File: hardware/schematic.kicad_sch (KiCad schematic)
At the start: 11 parts, among them J1 Connector_3, J2 Connector_2, J3 Connector_1, J4 Connector_4, J5 Connector_5, J6 Connector_6, U2 Nordic nRF52840 USB Dongle

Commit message: Small schematic update
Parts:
- removed J5: Connector_5, symbol Connector_Generic:Conn_01x03
- added J?: Connector_1, symbol Connector_Generic:Conn_01x04
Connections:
- net +5V: now also J?.1 (Pin_1)
- net Display-UART2_RX: now also J?.3 (Pin_3)
- net Display-UART2_TX: now also J?.2 (Pin_2)
- net GND: now also J?.4 (Pin_4)
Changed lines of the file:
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@@
+    (stroke (width 0) (type default) (color 0 0 0 0))
+  )
+  (wire (pts (xy 300.482 161.544) (xy 306.07 161.544))
     (stroke (width 0) (type default) (color 0 0 0 0))
   )
@@
   (label "SCLK" (at 184.8104 114.046 0)
     (effects (font (size 1.27 1.27)) (justify left bottom))
+  )
+  (label "+5V" (at 306.07 161.544 180)
+    (effects (font (size 1.27 1.27)) (justify right bottom))
   )
   (label "MISO" (at 285.3436 118.11 0)
@@
     (pin "1")
   )
-  (symbol (lib_id "Connector_Generic:Conn_01x03") (at 295.402 166.624 0) (mirror y) (unit 1)
-    (in_bom yes) (on_board yes)
-    (property "Reference" "J5" (id 0) (at 295.402 157.226 0)
-      (effects (font (size 1.27 1.27)) hide)
-    )
-    (property "Value" "Connector_5" (id 1) (at 292.1 167.132 90))
-    (property "Footprint" "" (id 2) (at 295.402 166.624 0)
-      (effects (font (size 1.27 1.27)) hide)
-    )
-    (property "Datasheet" "~" (id 3) (at 295.402 166.624 0)
+  (symbol (lib_id "Connector_Generic:Conn_01x04") (at 295.402 164.084 0) (mirror y) (unit 1)
+    (in_bom yes) (on_board yes)
+    (property "Reference" "J?" (id 0) (at 295.402 176.2252 0)
+      (effects (font (size 1.27 1.27)) hide)
+    )
+    (property "Value" "Connector_1" (id 1) (at 292.1 165.608 90))
+    (property "Footprint" "" (id 2) (at 295.402 164.084 0)
+      (effects (font (size 1.27 1.27)) hide)
+    )
+    (property "Datasheet" "~" (id 3) (at 295.402 164.084 0)
       (effects (font (size 1.27 1.27)) hide)
     )
@@
     (pin "2")
     (pin "3")
+    (pin "4")
   )
   (symbol (lib_id "Connector_Generic:Conn_01x02") (at 205.486 169.418 0) (mirror y) (unit 1)
@@
       (reference "J4") (unit 1) (value "Connector_4") (footprint "")
     )
-    (path "/3b6cb90e-f9fc-423a-bfb7-da052d8cf8af"
-      (reference "J5") (unit 1) (value "Connector_5") (footprint "")
-    )
     (path "/8de58a5f-d840-4c70-b7ae-d0148d4d329e"
       (reference "J6") (unit 1) (value "Connector_6") (footprint "")
     )
+    (path "/3b32823d-13b3-456f-8083-472773d66322"
+      (reference "J?") (unit 1) (value "Connector_1") (footprint "")
+    )
     (path "/00000000-0000-0000-0000-000062499af1"

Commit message: Removed not needed 2 pull up resistors. Corrected power for throttle, should be 3.3V
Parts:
- removed R2, R3: 100K, symbol Device:R
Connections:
- net +3.3V: now also J2.1 (Pin_1)
- net +5V: no longer J2.1 (Pin_1)

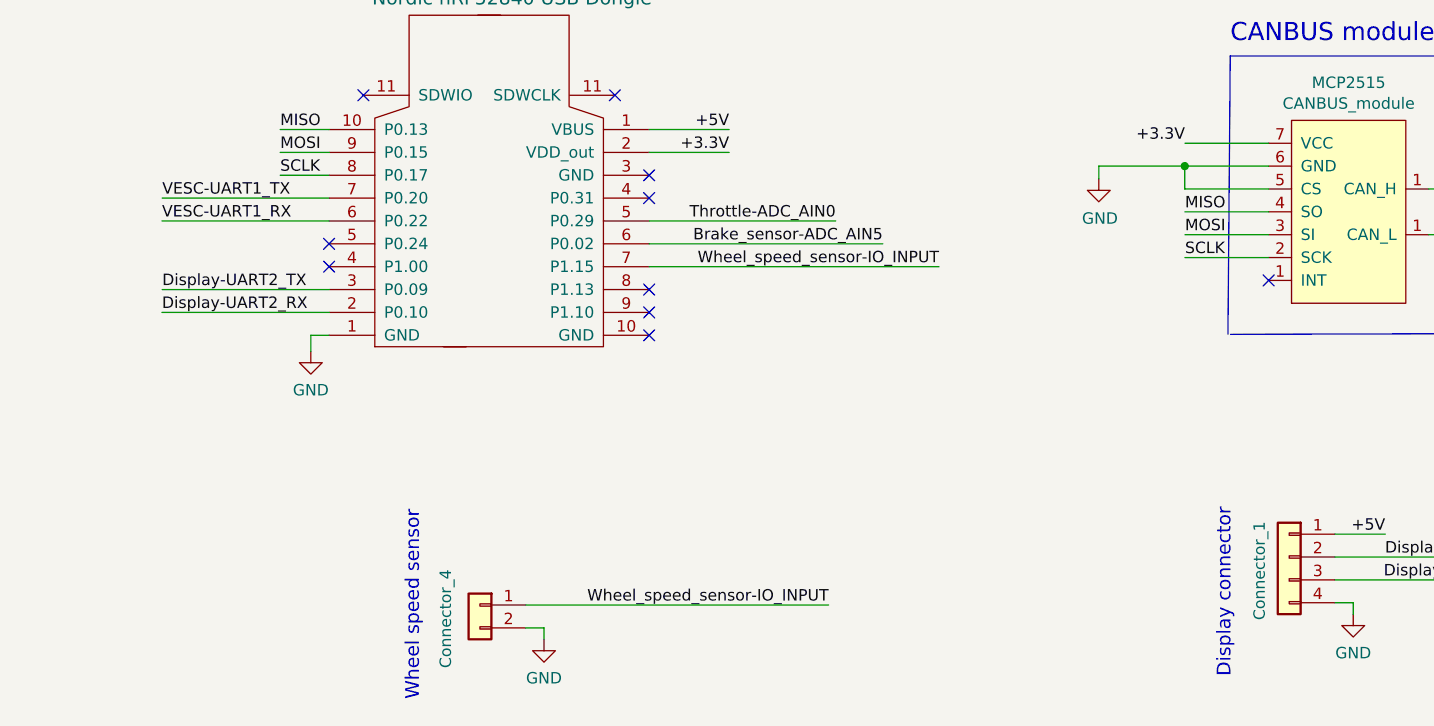
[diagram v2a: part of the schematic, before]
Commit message: Changed SPI pin to a more logical one - changed on firmware and on the schematic
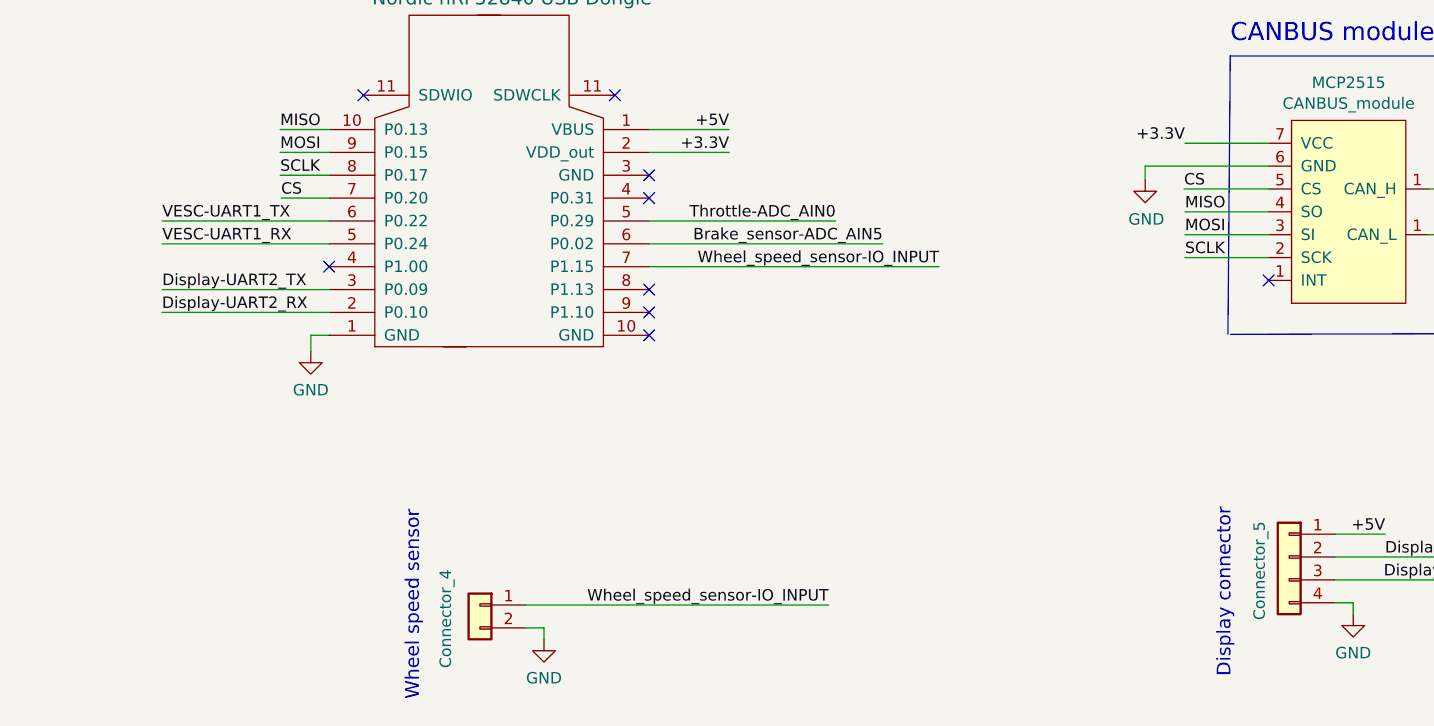
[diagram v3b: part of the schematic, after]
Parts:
- J?: value Connector_1 -> Connector_5
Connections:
- net GND: no longer MCP2515.5 (CS)
- net VESC-UART1_RX: now also U2.5 (P0.29); no longer U2.6 (P0.22)
- net VESC-UART1_TX: now also U2.6 (P0.22); no longer U2.7 (P1.15)
- new net CS: MCP2515.5 (CS), U2.7 (P1.15)
- no-connect marks 10 -> 9
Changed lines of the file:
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@@
 (kicad_sch (version 20211123) (generator eeschema)
   (paper "A3")
-  (junction (at 285.3182 113.03) (diameter 0) (color 0 0 0 0)
-  )
   (junction (at 126.492 129.794) (diameter 0) (color 0 0 0 0)
   )
-  (no_connect (at 190.246 121.666))
   (no_connect (at 221.996 105.156))
   (no_connect (at 294.64 125.73))
@@
     (stroke (width 0) (type default) (color 0 0 0 0))
   )
-  (wire (pts (xy 171.6786 119.126) (xy 190.246 119.126))
-    (stroke (width 0) (type default) (color 0 0 0 0))
-  )
-  (wire (pts (xy 275.7678 113.03) (xy 285.3182 113.03))
+  (wire (pts (xy 280.924 113.03) (xy 294.64 113.03))
     (stroke (width 0) (type default) (color 0 0 0 0))
   )
@@
     (stroke (width 0) (type default) (color 0 0 0 0))
   )
-  (wire (pts (xy 285.3182 113.03) (xy 294.64 113.03))
-    (stroke (width 0) (type default) (color 0 0 0 0))
-  )
   (polyline (pts (xy 290.3728 100.7872) (xy 290.1188 131.699))
     (stroke (width 0) (type default) (color 0 0 0 0))
@@
     (stroke (width 0) (type default) (color 0 0 0 0))
   )
-  (wire (pts (xy 285.3182 115.57) (xy 285.3182 113.03))
-    (stroke (width 0) (type default) (color 0 0 0 0))
-  )
   (wire (pts (xy 302.006 153.924) (xy 307.594 153.924))
     (stroke (width 0) (type default) (color 0 0 0 0))
@@
     (stroke (width 0) (type default) (color 0 0 0 0))
   )
-  (wire (pts (xy 275.7678 113.03) (xy 275.7678 114.4524))
+  (wire (pts (xy 280.924 113.03) (xy 280.924 114.554))
     (stroke (width 0) (type default) (color 0 0 0 0))
   )
@@
     (stroke (width 0) (type default) (color 0 0 0 0))
   )
+  (wire (pts (xy 190.246 116.586) (xy 184.912 116.586))
+    (stroke (width 0) (type default) (color 0 0 0 0))
+  )
   (wire (pts (xy 225.806 108.966) (xy 234.696 108.966))
     (stroke (width 0) (type default) (color 0 0 0 0))
@@
     (stroke (width 0) (type default) (color 0 0 0 0))
   )
+  (wire (pts (xy 171.704 121.666) (xy 190.246 121.666))
+    (stroke (width 0) (type default) (color 0 0 0 0))
+  )
+  (wire (pts (xy 171.704 119.126) (xy 190.246 119.126))
+    (stroke (width 0) (type default) (color 0 0 0 0))
+  )
   (wire (pts (xy 118.491 165.4048) (xy 120.523 165.4048))
     (stroke (width 0) (type default) (color 0 0 0 0))
@@
     (stroke (width 0) (type default) (color 0 0 0 0))
   )
-  (wire (pts (xy 285.3182 115.57) (xy 294.64 115.57))
-    (stroke (width 0) (type default) (color 0 0 0 0))
-  )
   (wire (pts (xy 312.42 115.57) (xy 326.39 115.57))
     (stroke (width 0) (type default) (color 0 0 0 0))
@@
     (stroke (width 0) (type default) (color 0 0 0 0))
   )
+  (wire (pts (xy 294.64 115.57) (xy 285.242 115.57))
+    (stroke (width 0) (type default) (color 0 0 0 0))
+  )
   (wire (pts (xy 118.237 101.9048) (xy 120.269 101.9048))
     (stroke (width 0) (type default) (color 0 0 0 0))
   )
   (wire (pts (xy 126.492 129.794) (xy 126.492 131.572))
-    (stroke (width 0) (type default) (color 0 0 0 0))
-  )
-  (wire (pts (xy 171.704 116.586) (xy 190.246 116.586))
     (stroke (width 0) (type default) (color 0 0 0 0))
   )
@@
     (effects (font (size 1.27 1.27)) (justify left bottom))
   )
-  (label "VESC-UART1_RX" (at 171.6786 119.126 0)
-    (effects (font (size 1.27 1.27)) (justify left bottom))
-  )
   (label "+5V" (at 123.825 94.2848 180)
     (effects (font (size 1.27 1.27)) (justify right bottom))
@@
     (effects (font (size 1.27 1.27)) (justify left bottom))
   )
+  (label "VESC-UART1_RX" (at 171.704 121.666 0)
+    (effects (font (size 1.27 1.27)) (justify left bottom))
+  )
   (label "CAN_H" (at 317.754 115.57 0)
     (effects (font (size 1.27 1.27)) (justify left bottom))
@@
     (effects (font (size 1.27 1.27)) (justify left bottom))
   )
+  (label "VESC-UART1_TX" (at 171.704 119.126 0)
+    (effects (font (size 1.27 1.27)) (justify left bottom))
+  )
   (label "VESC-UART1_RX" (at 135.763 96.8248 180)
     (effects (font (size 1.27 1.27)) (justify right bottom))
@@
     (effects (font (size 1.27 1.27)) (justify right bottom))
   )
-  (label "VESC-UART1_TX" (at 171.704 116.586 0)
-    (effects (font (size 1.27 1.27)) (justify left bottom))
-  )
   (label "Wheel_speed_sensor-IO_INPUT" (at 258.0132 124.206 180)
     (effects (font (size 1.27 1.27)) (justify right bottom))
   )
+  (label "CS" (at 184.912 116.586 0)
+    (effects (font (size 1.27 1.27)) (justify left bottom))
+  )
   (label "Throttle-ADC_AIN0" (at 246.5324 119.126 180)
     (effects (font (size 1.27 1.27)) (justify right bottom))
@@
   )
   (label "SCLK" (at 285.3436 123.19 0)
+    (effects (font (size 1.27 1.27)) (justify left bottom))
+  )
+  (label "CS" (at 285.242 115.57 0)
     (effects (font (size 1.27 1.27)) (justify left bottom))
   )
@@
     (pin "7")
   )
-  (symbol (lib_id "power:GND") (at 275.7678 114.4524 0) (unit 1)
-    (in_bom yes) (on_board yes)
-    (property "Reference" "#PWR04" (id 0) (at 275.7678 120.8024 0)
-      (effects (font (size 1.27 1.27)) hide)
-    )
-    (property "Value" "GND" (id 1) (at 275.8948 118.8466 0))
-    (property "Footprint" "" (id 2) (at 275.7678 114.4524 0)
-      (effects (font (size 1.27 1.27)) hide)
-    )
-    (property "Datasheet" "" (id 3) (at 275.7678 114.4524 0)
+  (symbol (lib_id "power:GND") (at 280.924 114.554 0) (unit 1)
+    (in_bom yes) (on_board yes)
+    (property "Reference" "#PWR04" (id 0) (at 280.924 120.904 0)
+      (effects (font (size 1.27 1.27)) hide)
+    )
+    (property "Value" "GND" (id 1) (at 281.051 118.9482 0))
+    (property "Footprint" "" (id 2) (at 280.924 114.554 0)
+      (effects (font (size 1.27 1.27)) hide)
+    )
+    (property "Datasheet" "" (id 3) (at 280.924 114.554 0)
       (effects (font (size 1.27 1.27)) hide)
     )
@@
       (effects (font (size 1.27 1.27)) hide)
     )
-    (property "Value" "Connector_1" (id 1) (at 293.624 157.988 90))
+    (property "Value" "Connector_5" (id 1) (at 293.624 157.988 90))
     (property "Footprint" "" (id 2) (at 296.926 156.464 0)
       (effects (font (size 1.27 1.27)) hide)
@@
     )
     (path "/3b32823d-13b3-456f-8083-472773d66322"
-      (reference "J?") (unit 1) (value "Connector_1") (footprint "")
+      (reference "J?") (unit 1) (value "Connector_5") (footprint "")
     )
     (path "/00000000-0000-0000-0000-000062499af1"

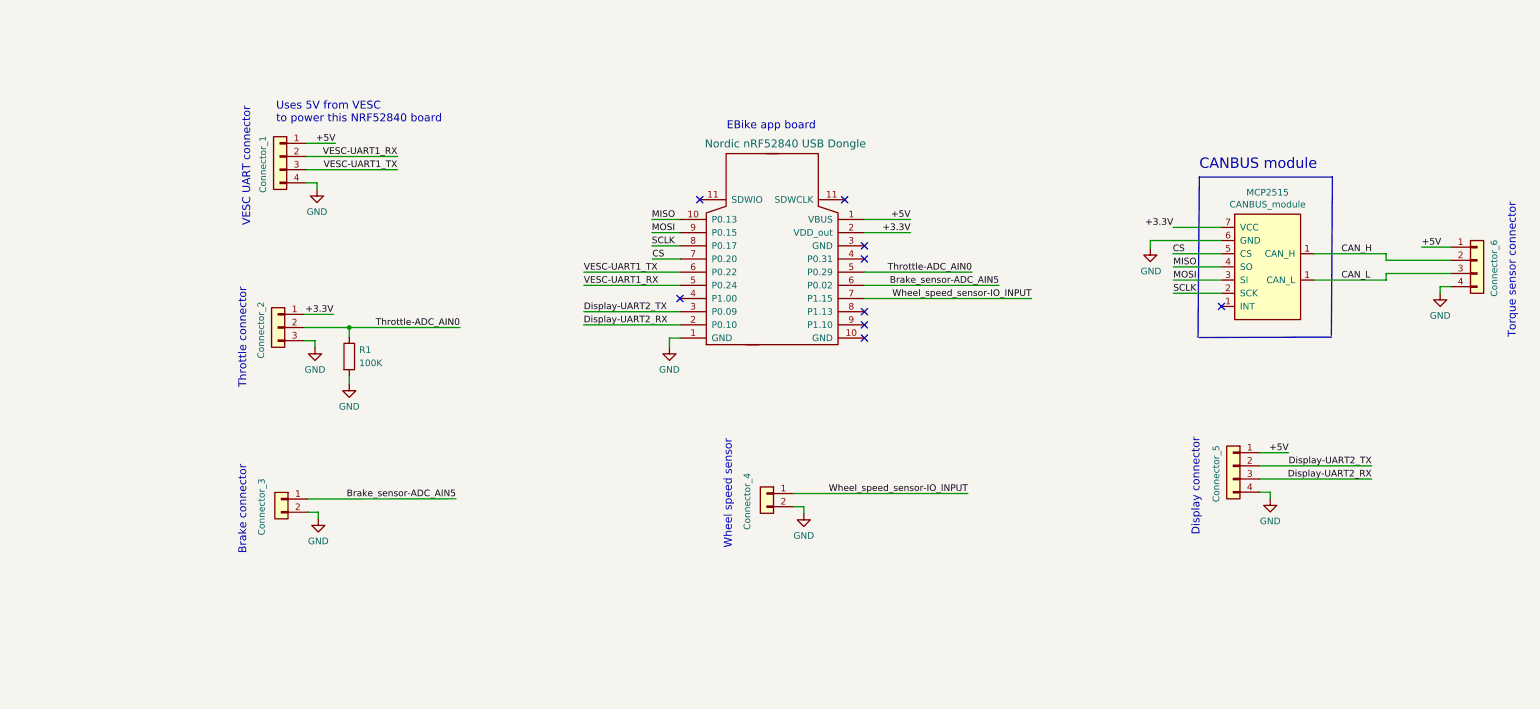
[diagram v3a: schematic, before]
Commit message: Updated schematic, added ESP32-S3 board and removed NRF52840. Added circuit to the motor temperature sensor (not tested).
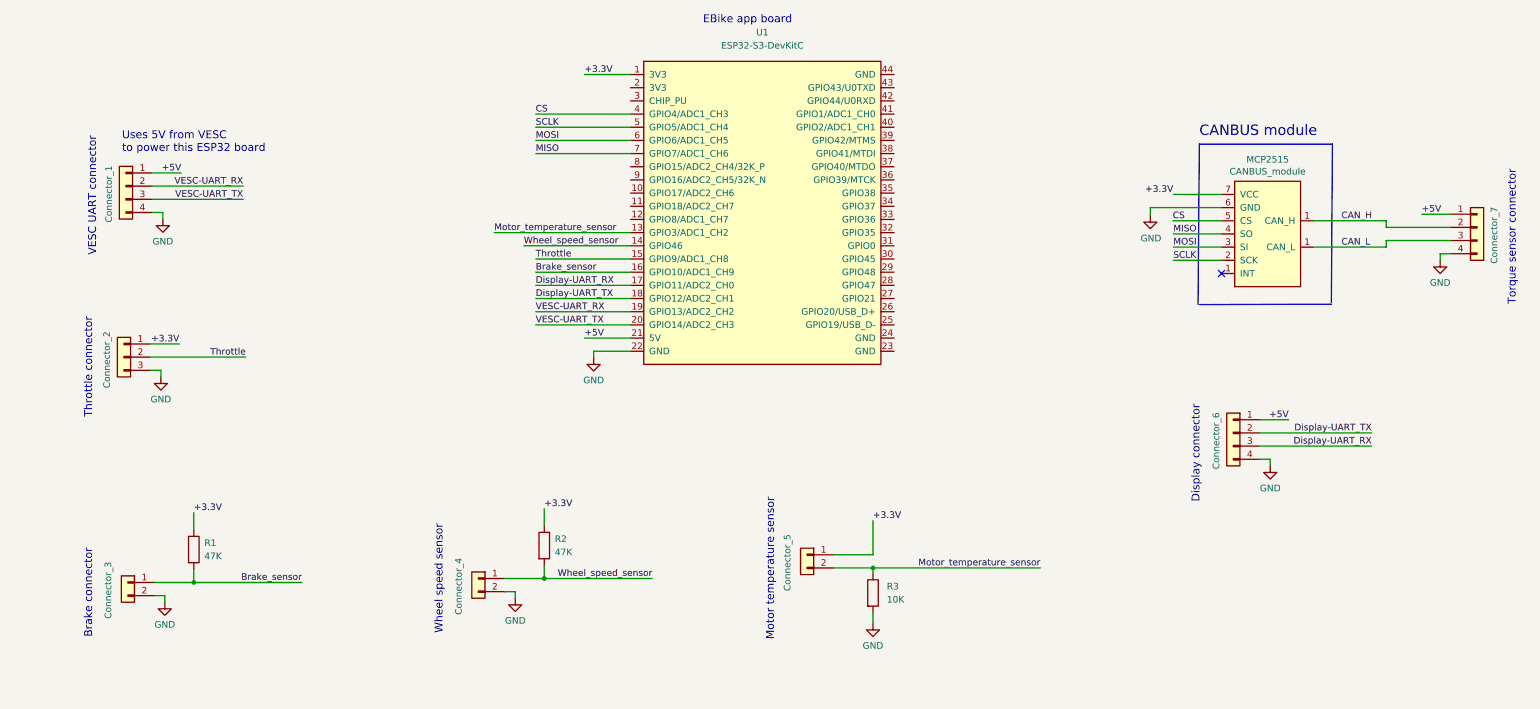
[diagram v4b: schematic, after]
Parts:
- removed U2: Nordic nRF52840 USB Dongle, symbol schematic-OLED_SPI-Bafang_M500_M600-rescue:Nordic_nRF52840_USB_Dongle-Wired_rem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
- added J5: Connector_5, symbol Connector_Generic:Conn_01x02
- added R2: 47K, symbol Device:R
- added R3: 10K, symbol Device:R
- added U1: ESP32-S3-DevKitC, Espressif:ESP32-S3-DevKitC, symbol Espressif:ESP32-S3-DevKitC
- J6: value Connector_6 -> Connector_7
- J7: renamed from J?; value Connector_5 -> Connector_6
- R1: value 100K -> 47K
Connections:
- net +3.3V: now also R1.1, J5.1 (Pin_1), R2.1, U1.1 (3V3)
- net +5V: now also U1.21 (5V)
- net CS: now also U1.4 (GPIO4/ADC1_CH3)
- net GND: now also R3.2, U1.22 (GND); no longer R1.2
- net MISO: now also U1.7 (GPIO7/ADC1_CH6)
- net MOSI: now also U1.6 (GPIO6/ADC1_CH5)
- net SCLK: now also U1.5 (GPIO5/ADC1_CH4)
- net Brake_sensor-ADC_AIN5 renamed Brake_sensor
- net Brake_sensor: now also R1.2, U1.16 (GPIO10/ADC1_CH9)
- net Display-UART2_RX renamed Display-UART_RX
- net Display-UART_RX: now also U1.17 (GPIO11/ADC2_CH0)
- net Display-UART2_TX renamed Display-UART_TX
- net Display-UART_TX: now also U1.18 (GPIO12/ADC2_CH1)
- net Throttle-ADC_AIN0 renamed Throttle
- net Throttle: now also U1.15 (GPIO9/ADC1_CH8); no longer R1.1
- net VESC-UART1_RX renamed VESC-UART_RX
- net VESC-UART_RX: now also U1.19 (GPIO13/ADC2_CH2)
- net VESC-UART1_TX renamed VESC-UART_TX
- net VESC-UART_TX: now also U1.20 (GPIO14/ADC2_CH3)
- net Wheel_speed_sensor-IO_INPUT renamed Wheel_speed_sensor
- net Wheel_speed_sensor: now also R2.2, U1.14 (GPIO46)
- new net Motor_temperature_sensor: J5.2 (Pin_2), R3.1, U1.13 (GPIO3/ADC1_CH2)
- no-connect marks 9 -> 1
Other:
- note added: "Motor temperature sensor"
- note added: "Uses 5V from VESC to power this ESP32 board"
- note removed: "Uses 5V from VESC to power this NRF52840 board"
- moved on the sheet: MCP2515

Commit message: Small update to schematic, adding no connected flags
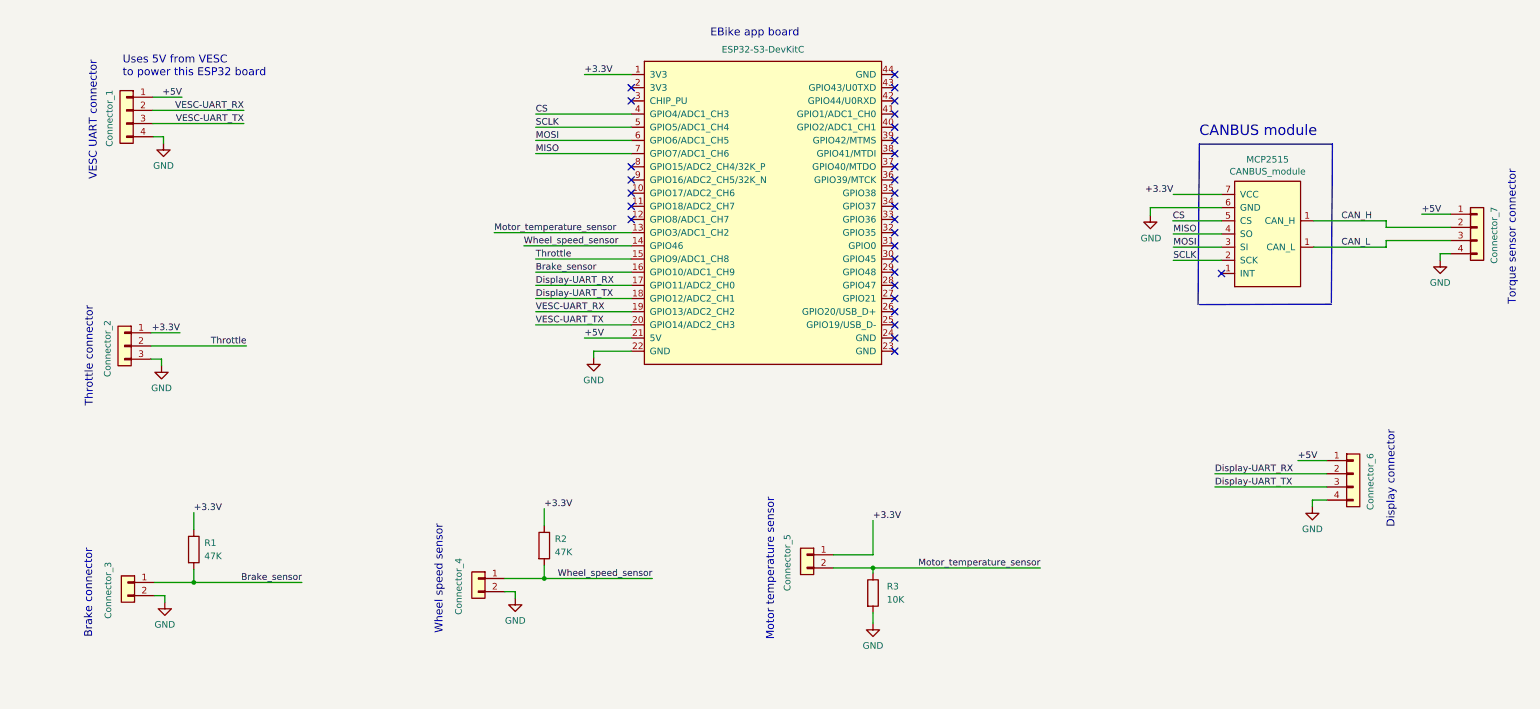
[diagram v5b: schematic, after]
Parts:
- removed J7: Connector_6, symbol Connector_Generic:Conn_01x04
- added J?: Connector_6, symbol Connector_Generic:Conn_01x04
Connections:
- net +5V: now also J?.1 (Pin_1)
- net Display-UART_RX: now also J?.2 (Pin_2)
- net Display-UART_TX: now also J?.3 (Pin_3)
- net GND: now also J?.4 (Pin_4)
- no-connect marks 1 -> 30
